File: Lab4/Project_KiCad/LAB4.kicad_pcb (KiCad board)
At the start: 2 copper layers, 50 x 50 mm, 38 parts, among them J1 Jumper 3, J3 jp5, J4 jp2, J5 Jumper 3, J6 Jumper 3, J7 Connector_3x2, J8 Connector_3x2, SW2 ON/OFF SWITCH, U1 AMS1117-3.3, U2 LM2776, U3 CP2102, U5 NE555

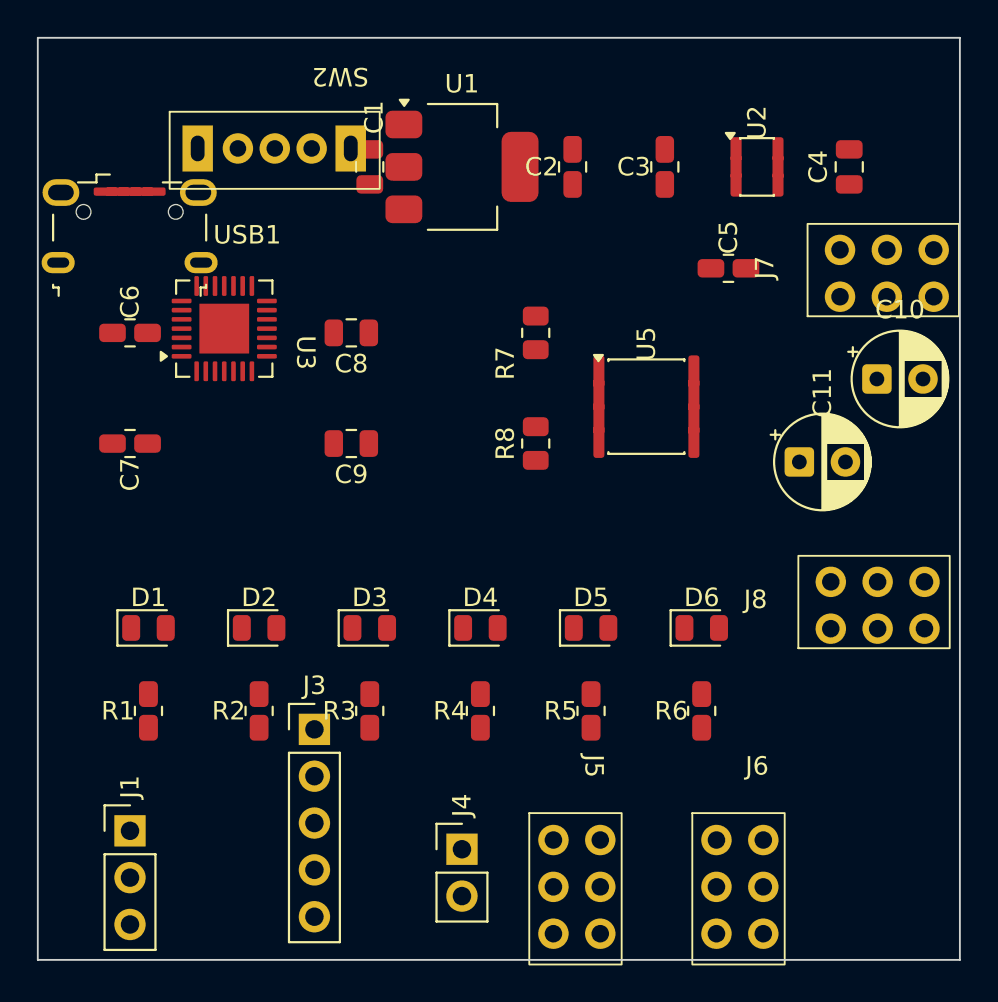
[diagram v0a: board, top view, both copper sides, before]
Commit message: update(Lab4): update report, pcb layout and add gui screenshots
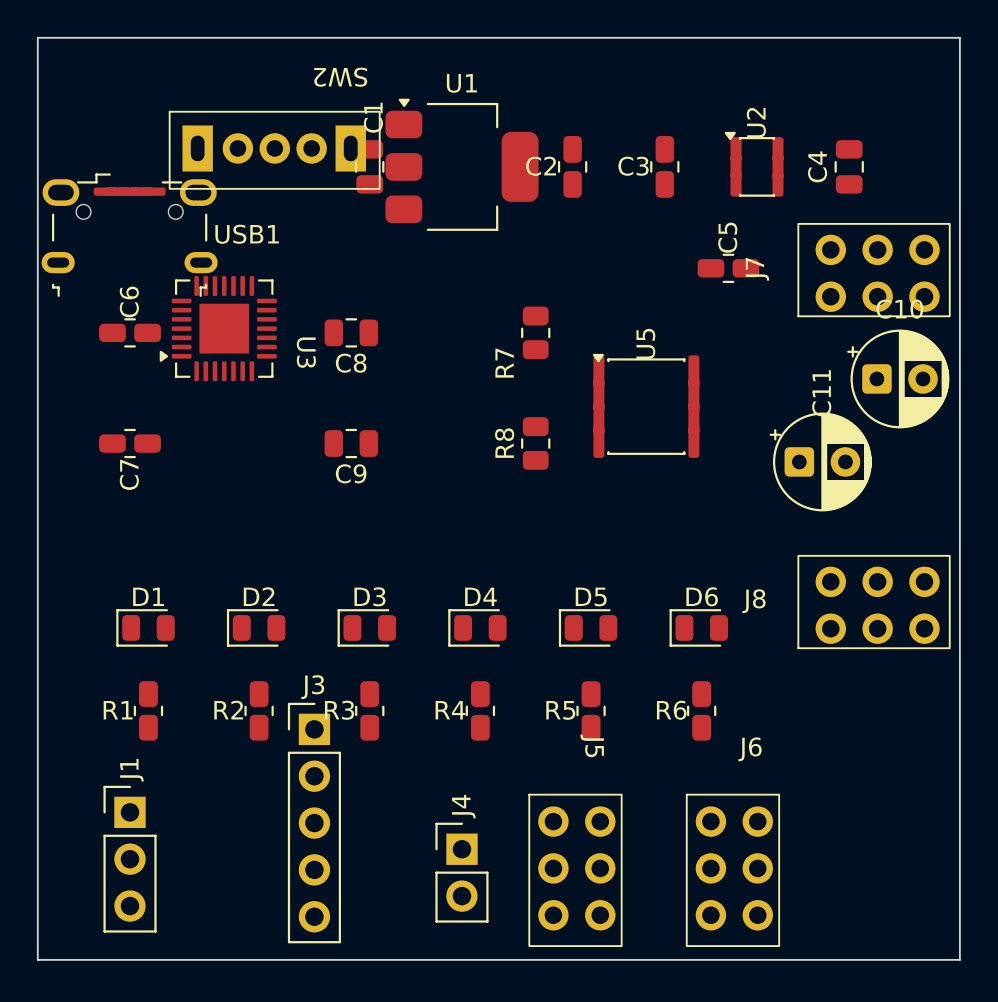
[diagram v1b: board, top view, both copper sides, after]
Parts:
- moved J6 1.04 mm to (63.7, 128.7)
- moved J1 1.00 mm to (30.0, 132.0)
- moved J5 1.00 mm to (55.2, 128.7)
- moved J7 0.50 mm to (64.4, 102.5)
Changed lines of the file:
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@@
 	(footprint "LAB3_CA1_14:Jumper 3"
 		(layer "F.Cu")
-		(at 64 129.65)
+		(at 63.7 128.65)
 		(property "Reference" "J6"
 			(at 0 -0.16 0)
@@
 	(footprint "Connector_PinHeader_2.54mm:PinHeader_1x03_P2.54mm_Vertical"
 		(layer "F.Cu")
-		(at 30 133)
+		(at 30 132)
 		(descr "Through hole straight pin header, 1x03, 2.54mm pitch, single row")
 		(tags "Through hole pin header THT 1x03 2.54mm single row")
@@
 	(footprint "LAB3_CA1_14:Connector 3x2"
 		(layer "F.Cu")
-		(at 64.92 102.46 90)
+		(at 64.42 102.46 90)
 		(property "Reference" "J7"
 			(at 0 -0.5 90)
@@
 	(footprint "LAB3_CA1_14:Jumper 3"
 		(layer "F.Cu")
-		(at 55.16 129.65)
+		(at 55.16 128.65)
 		(property "Reference" "J5"
 			(at 0 -0.16 270)
@@
 		)
 		(fp_text user "${REFERENCE}"
-			(at 0 5.79 270)
+			(at 0.34 2.85 270)
 			(unlocked yes)
 			(layer "F.Fab")
